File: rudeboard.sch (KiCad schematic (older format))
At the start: 132 parts, among them SW1 SW_Push, U1 Elite-C

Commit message: finish footprints/routing
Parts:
- removed SW1: SW_Push, LED_THT:LED_D3.0mm, symbol Switch:SW_Push
- MX1, MX10, MX11, MX12, MX13, MX14, MX15, MX16, MX17, MX18, MX19, MX2, MX20, MX21, MX22, MX23, MX24, MX25, MX26, MX27, MX28, MX29, MX3, MX30, MX31, MX32, MX33, MX34, MX35, MX36, MX37, MX38, MX39, MX4, MX40, MX41, MX42, MX43, MX44, MX45, MX46, MX49, MX5, MX50, MX51, MX52, MX53, MX54, MX56, MX6, MX60, MX61, MX7, MX8, MX9: footprint MX_Alps_Hybrid:MX-1U -> MX_Alps_Hybrid:MX-1U-NoLED
- MX47, MX55, MX57, MX59, MX62: footprint MX_Alps_Hybrid:MX-1U -> MX_Alps_Hybrid:MX-1.5U-NoLED
- MX48: footprint MX_Alps_Hybrid:MX-1U -> MX_Alps_Hybrid:MX-ISO
- MX58: footprint MX_Alps_Hybrid:MX-1U -> MX_Alps_Hybrid:MX-1.75U-NoLED
- MX63, MX64, MX65: footprint MX_Alps_Hybrid:MX-1U -> MX_Alps_Hybrid:MX-3U-NoLED
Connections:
- net col0: now also MX43.1 (COL); no longer MX45.1 (COL)
- net col1: now also MX45.1 (COL); no longer MX47.1 (COL)
- net col2: now also MX47.1 (COL), U1.13 (10/PB6); no longer MX49.1 (COL), U1.18 (A1/PF6)
- net col3: now also MX49.1 (COL); no longer MX51.1 (COL)
- net col4: now also MX51.1 (COL); no longer MX53.1 (COL)
- net col5: now also MX53.1 (COL), U1.29 (F0); no longer MX43.1 (COL), U1.15 (14/PB3)
- net row0: now also U1.12 (9/PB5); no longer U1.5 (2/PD1)
- net row1: now also U1.25 (B7); no longer U1.6 (3/PD0)
- net row2: now also U1.11 (8/PB4); no longer U1.7 (4/PD4)
- net row3: now also U1.10 (7/PE6); no longer U1.8 (5/PC6)
- net row5: now also U1.8 (5/PC6); no longer U1.10 (7/PE6)
- net row6: now also U1.7 (4/PD4); no longer U1.11 (8/PB4)
- net row7: now also U1.18 (A1/PF6); no longer U1.12 (9/PB5)
- net row8: now also U1.5 (2/PD1); no longer U1.25 (B7)
- net row9: now also U1.6 (3/PD0); no longer U1.26 (D5)
- net at MX47.2 (ROW): now also D47.2 (A); no longer D46.2 (A)
- net at MX46.2 (ROW): now also D46.2 (A); no longer D45.2 (A)
- net at MX45.2 (ROW): now also D45.2 (A); no longer D44.2 (A)
- net at MX44.2 (ROW): now also D44.2 (A); no longer D43.2 (A)
- net at MX51.2 (ROW): now also D51.2 (A); no longer D50.2 (A)
- net at MX50.2 (ROW): now also D50.2 (A); no longer D49.2 (A)
- net at MX49.2 (ROW): now also D49.2 (A); no longer D48.2 (A)
- net at MX48.2 (ROW): now also D48.2 (A); no longer D47.2 (A)
- net at MX43.2 (ROW): now also D43.2 (A); no longer D54.2 (A)
- net at MX54.2 (ROW): now also D54.2 (A); no longer D53.2 (A)
- net at MX53.2 (ROW): now also D53.2 (A); no longer D52.2 (A)
- net at MX52.2 (ROW): now also D52.2 (A); no longer D51.2 (A)
- removed net GND: U1.23 (GND), U1.3 (GND), U1.4 (GND)
- no-connect marks 8 -> 12
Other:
- moved on the sheet: MX43, MX44, MX45, MX46, MX47, MX48, MX49, MX50, MX51, MX52, MX53, MX54

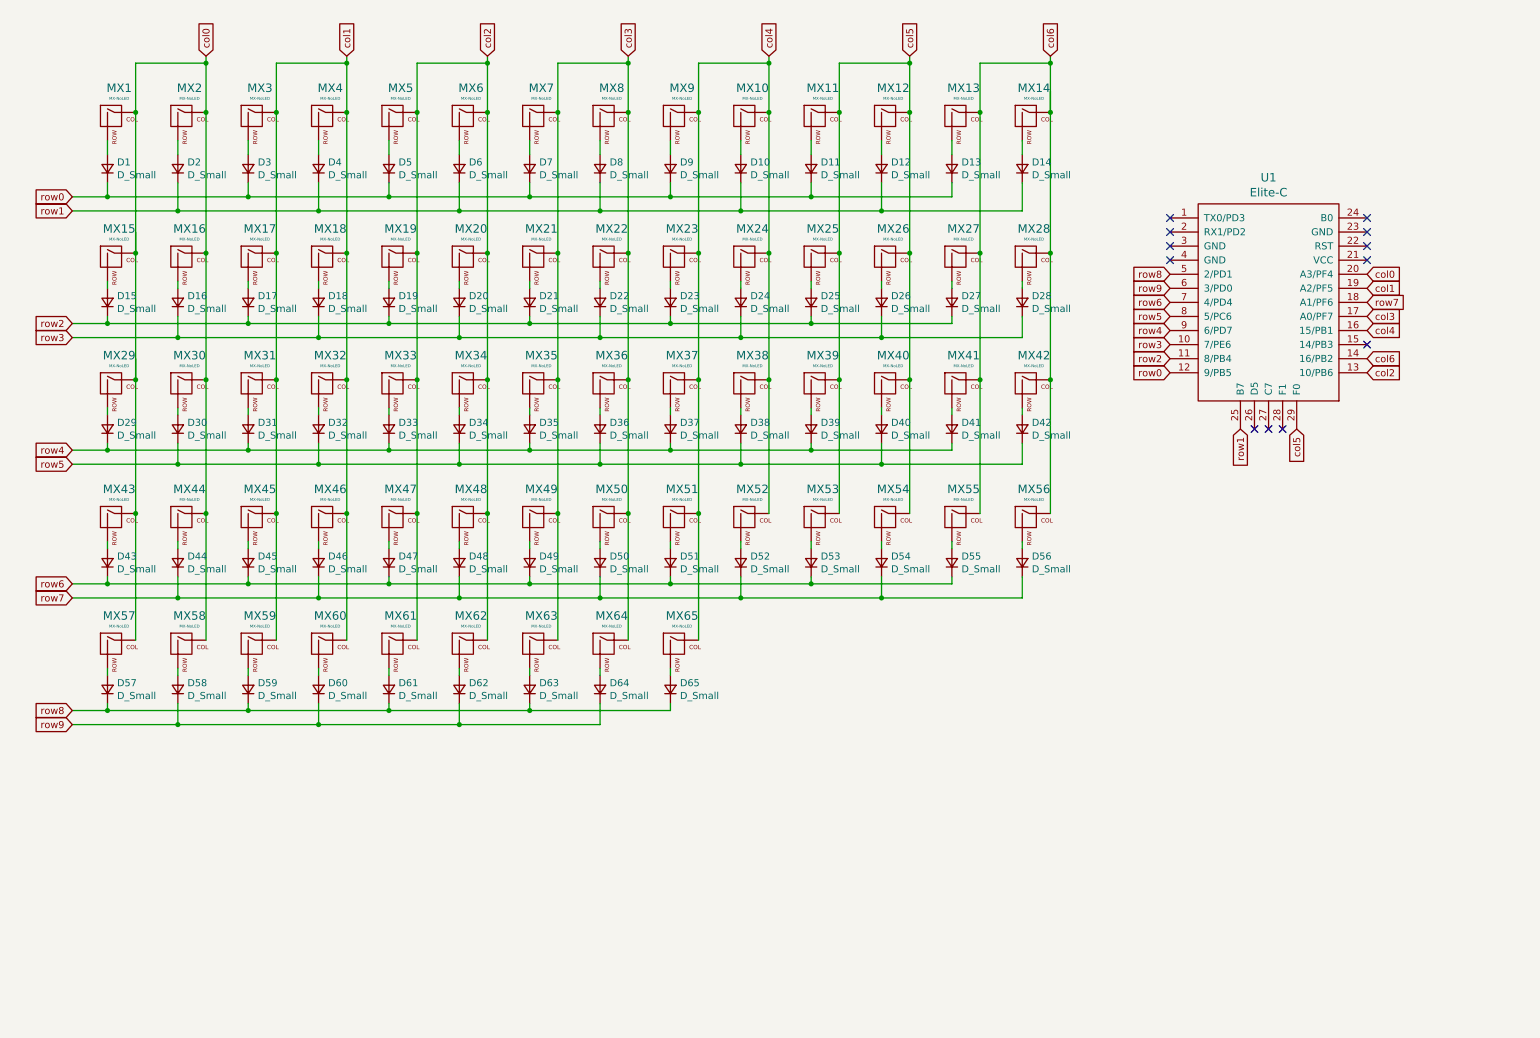
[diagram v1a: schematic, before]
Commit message: update to v1.1
changes to schematic:
- potentially better
- more pins used so more dependant on elite-c but more legible

routing:
- looks better than before
- is more dependant on elite-c (or much less on pro micro)

update revision/dates
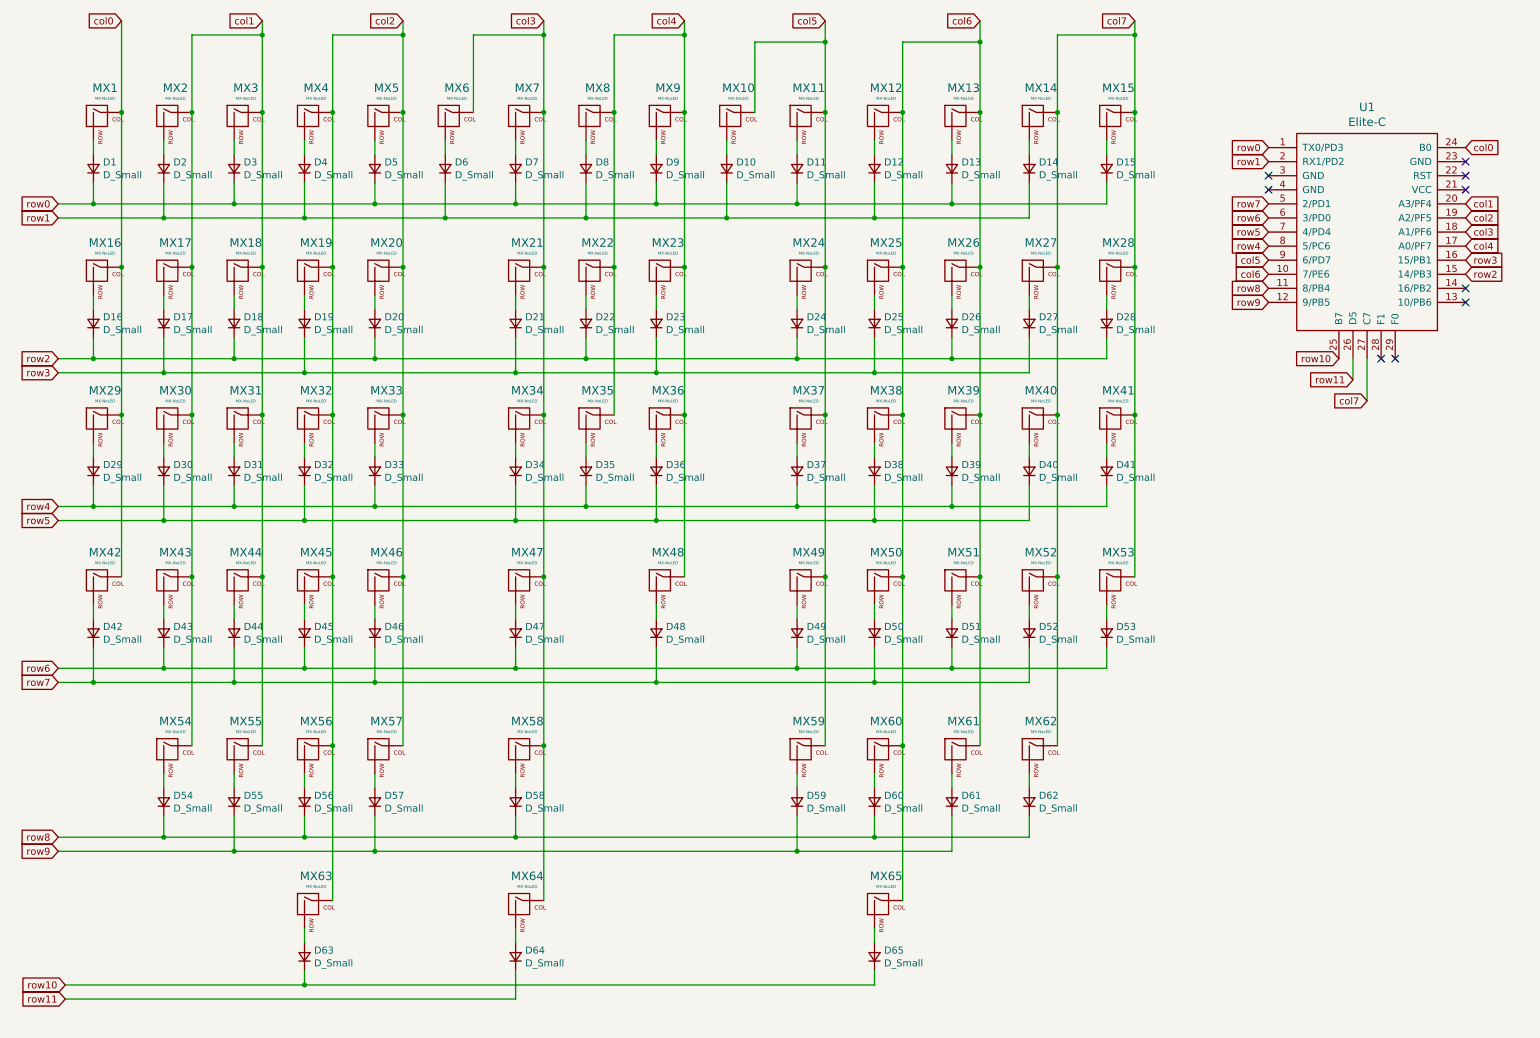
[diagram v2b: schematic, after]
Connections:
- net col0: now also MX42.1 (COL), U1.24 (B0); no longer MX15.1 (COL), MX2.1 (COL), MX30.1 (COL), MX43.1 (COL), MX44.1 (COL), MX57.1 (COL), MX58.1 (COL), U1.20 (A3/PF4)
- net col1: now also MX2.1 (COL), MX30.1 (COL), MX43.1 (COL), MX44.1 (COL), MX54.1 (COL), MX55.1 (COL), U1.20 (A3/PF4); no longer MX32.1 (COL), MX4.1 (COL), MX45.1 (COL), MX46.1 (COL), MX59.1 (COL), MX60.1 (COL), U1.19 (A2/PF5)
- net col2: now also MX32.1 (COL), MX4.1 (COL), MX45.1 (COL), MX46.1 (COL), MX56.1 (COL), MX57.1 (COL), MX63.1 (COL), U1.19 (A2/PF5); no longer MX34.1 (COL), MX47.1 (COL), MX48.1 (COL), MX6.1 (COL), MX61.1 (COL), MX62.1 (COL), U1.13 (10/PB6)
- net col3: now also MX34.1 (COL), MX47.1 (COL), MX58.1 (COL), MX6.1 (COL), U1.18 (A1/PF6); no longer MX22.1 (COL), MX35.1 (COL), MX36.1 (COL), MX49.1 (COL), MX50.1 (COL), MX63.1 (COL), MX8.1 (COL), U1.17 (A0/PF7)
- net col4: now also MX22.1 (COL), MX35.1 (COL), MX36.1 (COL), MX48.1 (COL), MX8.1 (COL), U1.17 (A0/PF7); no longer MX10.1 (COL), MX24.1 (COL), MX37.1 (COL), MX38.1 (COL), MX51.1 (COL), MX52.1 (COL), MX65.1 (COL), U1.16 (15/PB1)
- net col5: now also MX10.1 (COL), MX24.1 (COL), MX37.1 (COL), MX49.1 (COL), MX59.1 (COL), U1.9 (6/PD7); no longer MX12.1 (COL), MX25.1 (COL), MX26.1 (COL), MX39.1 (COL), MX40.1 (COL), MX53.1 (COL), MX54.1 (COL), U1.29 (F0)
- net col6: now also MX12.1 (COL), MX25.1 (COL), MX26.1 (COL), MX38.1 (COL), MX39.1 (COL), MX50.1 (COL), MX51.1 (COL), MX60.1 (COL), MX61.1 (COL), MX65.1 (COL), U1.10 (7/PE6); no longer MX14.1 (COL), MX27.1 (COL), MX28.1 (COL), MX41.1 (COL), MX42.1 (COL), MX55.1 (COL), MX56.1 (COL), U1.14 (16/PB2)
- net row0: now also D15.1 (K), U1.1 (TX0/PD3); no longer U1.12 (9/PB5)
- net row1: now also U1.2 (RX1/PD2); no longer U1.25 (B7)
- net row2: now also D16.1 (K), D18.1 (K), D20.1 (K), D22.1 (K), D24.1 (K), D26.1 (K), D28.1 (K), U1.15 (14/PB3); no longer D15.1 (K), D17.1 (K), D19.1 (K), D21.1 (K), D23.1 (K), D25.1 (K), D27.1 (K), U1.11 (8/PB4)
- net row3: now also D17.1 (K), D19.1 (K), D21.1 (K), D23.1 (K), D25.1 (K), D27.1 (K), U1.16 (15/PB1); no longer D16.1 (K), D18.1 (K), D20.1 (K), D22.1 (K), D24.1 (K), D26.1 (K), D28.1 (K), U1.10 (7/PE6)
- net row4: now also U1.8 (5/PC6); no longer U1.9 (6/PD7)
- net row5: now also U1.7 (4/PD4); no longer D42.1 (K), U1.8 (5/PC6)
- net row6: now also U1.6 (3/PD0); no longer D55.1 (K), U1.7 (4/PD4)
- net row7: now also D42.1 (K), U1.5 (2/PD1); no longer D54.1 (K), D56.1 (K), U1.18 (A1/PF6)
- net row8: now also D54.1 (K), D56.1 (K), D58.1 (K), D60.1 (K), D62.1 (K), U1.11 (8/PB4); no longer D57.1 (K), D59.1 (K), D61.1 (K), D63.1 (K), D65.1 (K), U1.5 (2/PD1)
- net row9: now also D55.1 (K), D57.1 (K), D59.1 (K), D61.1 (K), U1.12 (9/PB5); no longer D58.1 (K), D60.1 (K), D62.1 (K), D64.1 (K), U1.6 (3/PD0)
- net row11: now reaches U1.26 (D5)
- net row11: now also D64.1 (K)
- net col7: now reaches U1.27 (C7)
- net col7: now also MX14.1 (COL), MX15.1 (COL), MX27.1 (COL), MX28.1 (COL), MX40.1 (COL), MX41.1 (COL), MX52.1 (COL), MX53.1 (COL), MX62.1 (COL)
- new net row10: D63.1 (K), D65.1 (K), U1.25 (B7)
- no-connect marks 12 -> 9
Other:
- moved on the sheet: U1

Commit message: rerouted pcb
- better placement of elite-c
- looks better
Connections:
- net col1: now also U1.18 (A1/PF6); no longer U1.20 (A3/PF4)
- net col2: now also U1.17 (A0/PF7); no longer U1.19 (A2/PF5)
- net col3: now also U1.16 (15/PB1); no longer U1.18 (A1/PF6)
- net col4: now also U1.15 (14/PB3); no longer U1.17 (A0/PF7)
- net col6: now also U1.8 (5/PC6); no longer U1.10 (7/PE6)
- net col7: now also U1.7 (4/PD4); no longer U1.27 (C7)
- net row10: now also U1.11 (8/PB4); no longer U1.25 (B7)
- net row11: now also U1.10 (7/PE6); no longer U1.26 (D5)
- net row2: now also U1.19 (A2/PF5); no longer U1.15 (14/PB3)
- net row3: now also U1.20 (A3/PF4); no longer U1.16 (15/PB1)
- net row4: now also U1.28 (F1); no longer U1.8 (5/PC6)
- net row5: now also U1.29 (F0); no longer U1.7 (4/PD4)
- net row6: now also U1.26 (D5); no longer U1.6 (3/PD0)
- net row7: now also U1.27 (C7); no longer U1.5 (2/PD1)
- net row8: now also U1.25 (B7); no longer U1.11 (8/PB4)
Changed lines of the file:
@@
 NoConn ~ 10750 1650
 NoConn ~ 10750 1550
-Text GLabel 10750 2250 2    50   Input ~ 0
+Text GLabel 10750 1850 2    50   Input ~ 0
 row3
 NoConn ~ 10750 1750
-NoConn ~ 10150 2950
-NoConn ~ 10250 2950
-Text GLabel 9350 2450 0    50   Input ~ 0
+Text GLabel 9850 2950 0    50   Input ~ 0
 row8
 $Comp
@@
 	1    0    0    -1
 $EndComp
-Text GLabel 9350 2350 0    50   Input ~ 0
+Text GLabel 9350 2150 0    50   Input ~ 0
 col6
 Text GLabel 9350 2250 0    50   Input ~ 0
 col5
+Text GLabel 10750 2350 2    50   Input ~ 0
+col4
 Text GLabel 10750 2150 2    50   Input ~ 0
-col4
+col2
 Text GLabel 10750 2050 2    50   Input ~ 0
-col3
-Text GLabel 10750 1950 2    50   Input ~ 0
-col2
-Text GLabel 10750 1850 2    50   Input ~ 0
 col1
 Text GLabel 10750 1450 2    50   Input ~ 0
 col0
-Text GLabel 9350 1850 0    50   Input ~ 0
+Text GLabel 10050 3250 0    50   Input ~ 0
 row7
-Text GLabel 9350 1950 0    50   Input ~ 0
+Text GLabel 9950 3100 0    50   Input ~ 0
 row6
-Text GLabel 9350 2050 0    50   Input ~ 0
+Text GLabel 10250 3550 0    50   Input ~ 0
 row5
-Text GLabel 9350 2150 0    50   Input ~ 0
+Text GLabel 10150 3400 0    50   Input ~ 0
 row4
-Text GLabel 10750 2350 2    50   Input ~ 0
+Text GLabel 10750 1950 2    50   Input ~ 0
 row2
 Text GLabel 9350 1550 0    50   Input ~ 0
@@
 Text GLabel 9350 2550 0    50   Input ~ 0
 row9
-Text GLabel 10050 3250 0    50   Input ~ 0
+Text GLabel 9350 2050 0    50   Input ~ 0
 col7
-Text GLabel 9850 2950 0    50   Input ~ 0
+Text GLabel 9350 2450 0    50   Input ~ 0
 row10
-Text GLabel 9950 3100 0    50   Input ~ 0
+Text GLabel 9350 2350 0    50   Input ~ 0
 row11
 Wire Wire Line
@@
 Text GLabel 800  7500 0    50   Input ~ 0
 row11
+Wire Wire Line
+	10050 2950 10050 3250
+Text GLabel 10750 2250 2    50   Input ~ 0
+col3
+Wire Wire Line
+	10150 3400 10150 2950
+Wire Wire Line
+	10250 3550 10250 2950
 NoConn ~ 10750 2550
-Wire Wire Line
-	10050 2950 10050 3250
 NoConn ~ 10750 2450
+NoConn ~ 9350 1850
+NoConn ~ 9350 1950
 $EndSCHEMATC

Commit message: update iso enter to 0deg rotated
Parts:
- MX48: footprint MX_Alps_Hybrid:MX-ISO -> Button_Switch_Keyboard:SW_Cherry_MX_ISOEnter_PCB
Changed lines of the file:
@@
 F 0 "MX48" H 5083 4773 60  0000 C CNN
 F 1 "MX-NoLED" H 5083 4699 20  0000 C CNN
-F 2 "MX_Alps_Hybrid:MX-ISO" H 4425 4525 60  0001 C CNN
+F 2 "Button_Switch_Keyboard:SW_Cherry_MX_ISOEnter_PCB" H 4425 4525 60  0001 C CNN
 F 3 "" H 4425 4525 60  0001 C CNN
 	1    5050 4550
